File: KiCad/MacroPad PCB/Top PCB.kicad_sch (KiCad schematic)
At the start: 28 parts, among them J1 Conn_02x06_Counter_Clockwise, SW1 SW_MEC_5G, U1 SeeeduinoXIAO

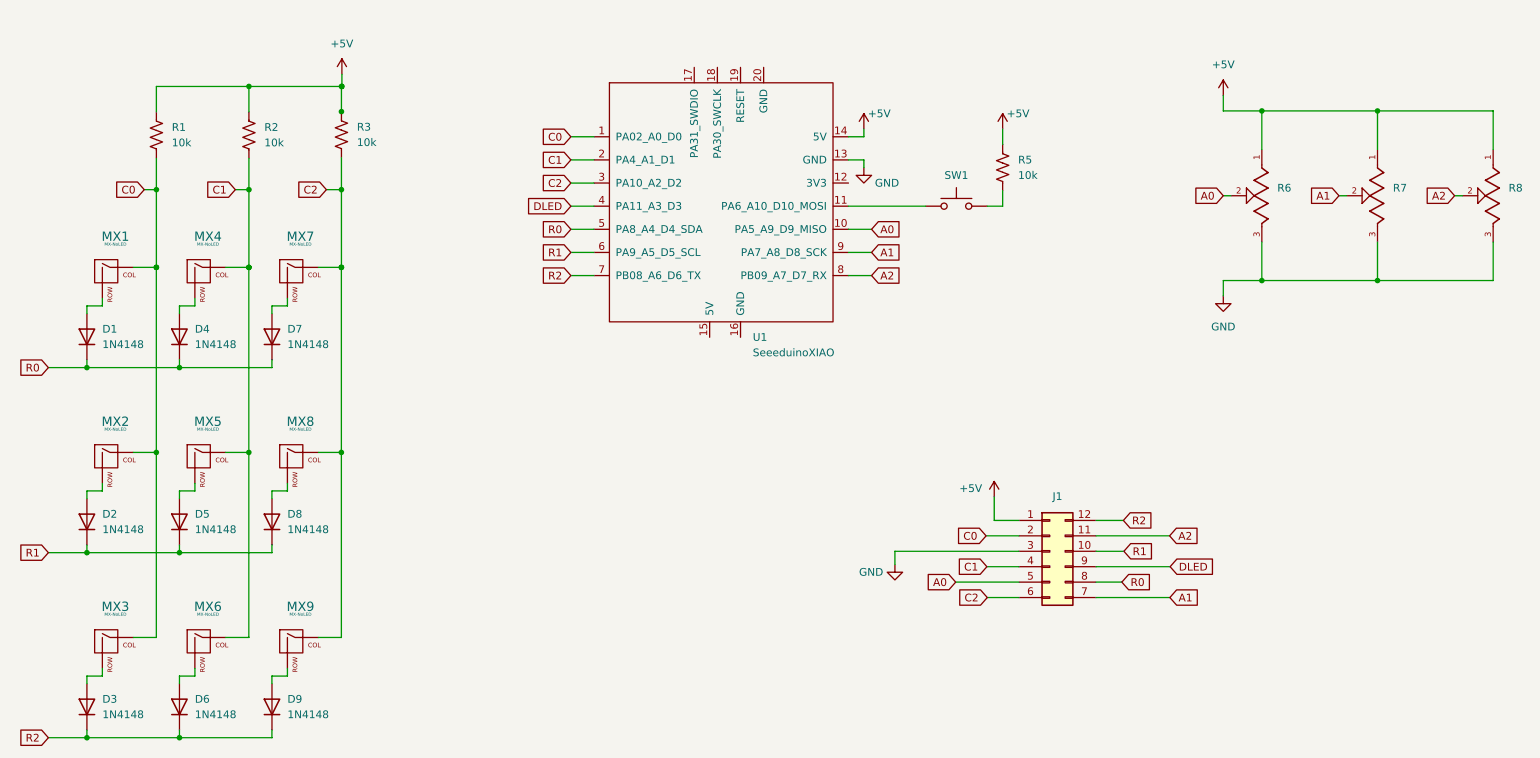
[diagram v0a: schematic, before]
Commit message: Begin writing firmware, fix PCB to use 3.3V logic level
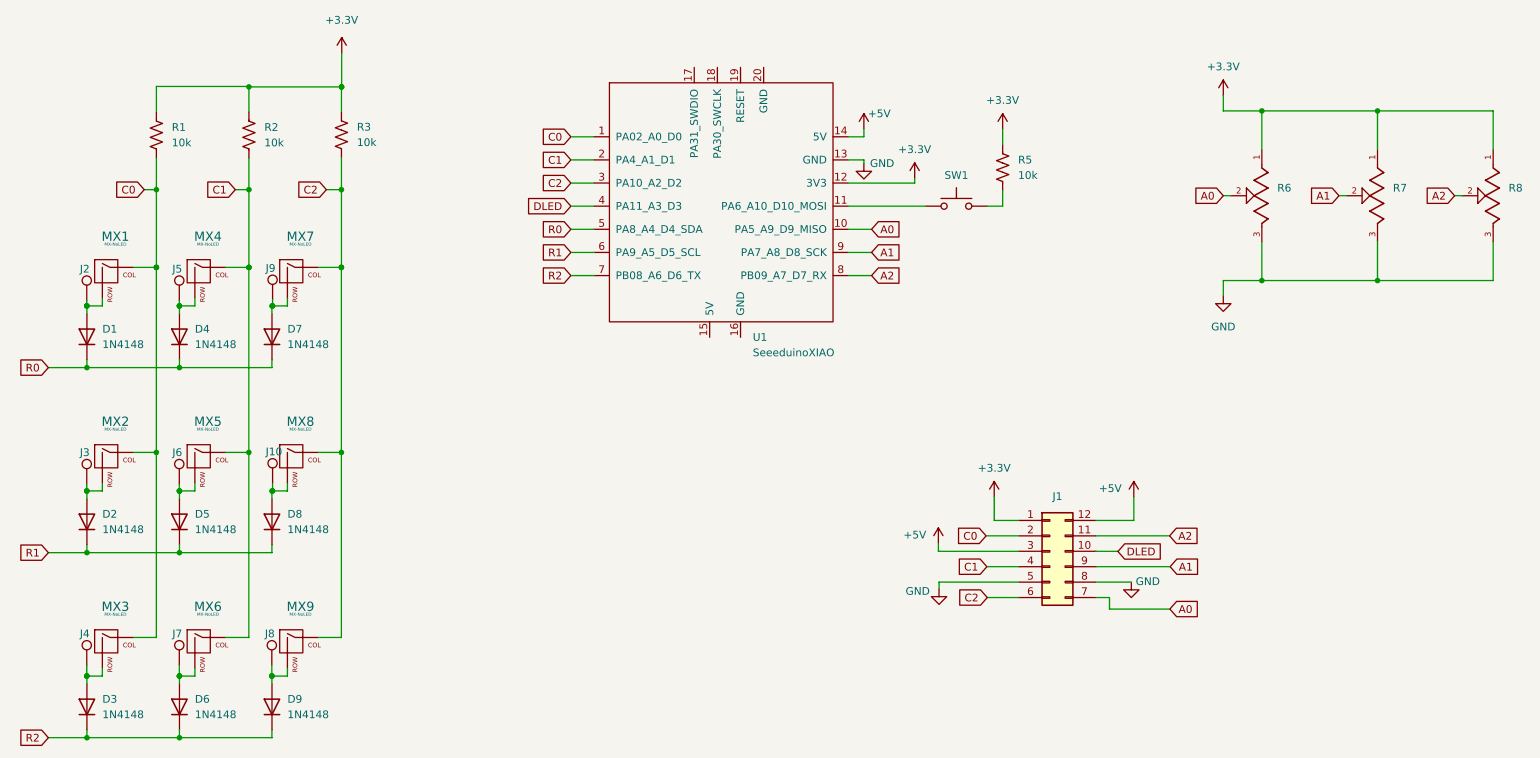
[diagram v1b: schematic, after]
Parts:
- added J10, J2, J3, J4, J5, J6, J7, J8, J9: TestPoint, TestPoint:TestPoint_Pad_2.0x2.0mm, symbol Connector:TestPoint
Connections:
- net +5V: now also J1.12 (Pin_12), J1.3 (Pin_3); no longer J1.1 (Pin_1), R1.1, R2.1, R3.2, R5.2, R6.1, R7.1, R8.1
- net A0: now also J1.7 (Pin_7); no longer J1.5 (Pin_5)
- net A1: now also J1.9 (Pin_9); no longer J1.7 (Pin_7)
- net DLED: now also J1.10 (Pin_10); no longer J1.9 (Pin_9)
- net GND: now also J1.5 (Pin_5), J1.8 (Pin_8); no longer J1.3 (Pin_3)
- net R0: no longer J1.8 (Pin_8)
- net R1: no longer J1.10 (Pin_10)
- net R2: no longer J1.12 (Pin_12)
- net at D6.2 (A), MX6.2 (ROW): now also J7.1
- net +3.3V: now reaches U1.12 (3V3)
- net +3.3V: now also J1.1 (Pin_1), R1.1, R2.1, R3.2, R5.2, R6.1, R7.1, R8.1
- net at D3.2 (A), MX3.2 (ROW): now also J4.1
- net at D5.2 (A), MX5.2 (ROW): now also J6.1
- net at D2.2 (A), MX2.2 (ROW): now also J3.1
- net at D4.2 (A), MX4.2 (ROW): now also J5.1
- net at D9.2 (A), MX9.2 (ROW): now also J8.1
- net at D8.2 (A), MX8.2 (ROW): now also J10.1
- net at D7.2 (A), MX7.2 (ROW): now also J9.1
- net at D1.2 (A), MX1.2 (ROW): now also J2.1
